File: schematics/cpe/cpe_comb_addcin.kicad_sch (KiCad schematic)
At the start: 9 parts

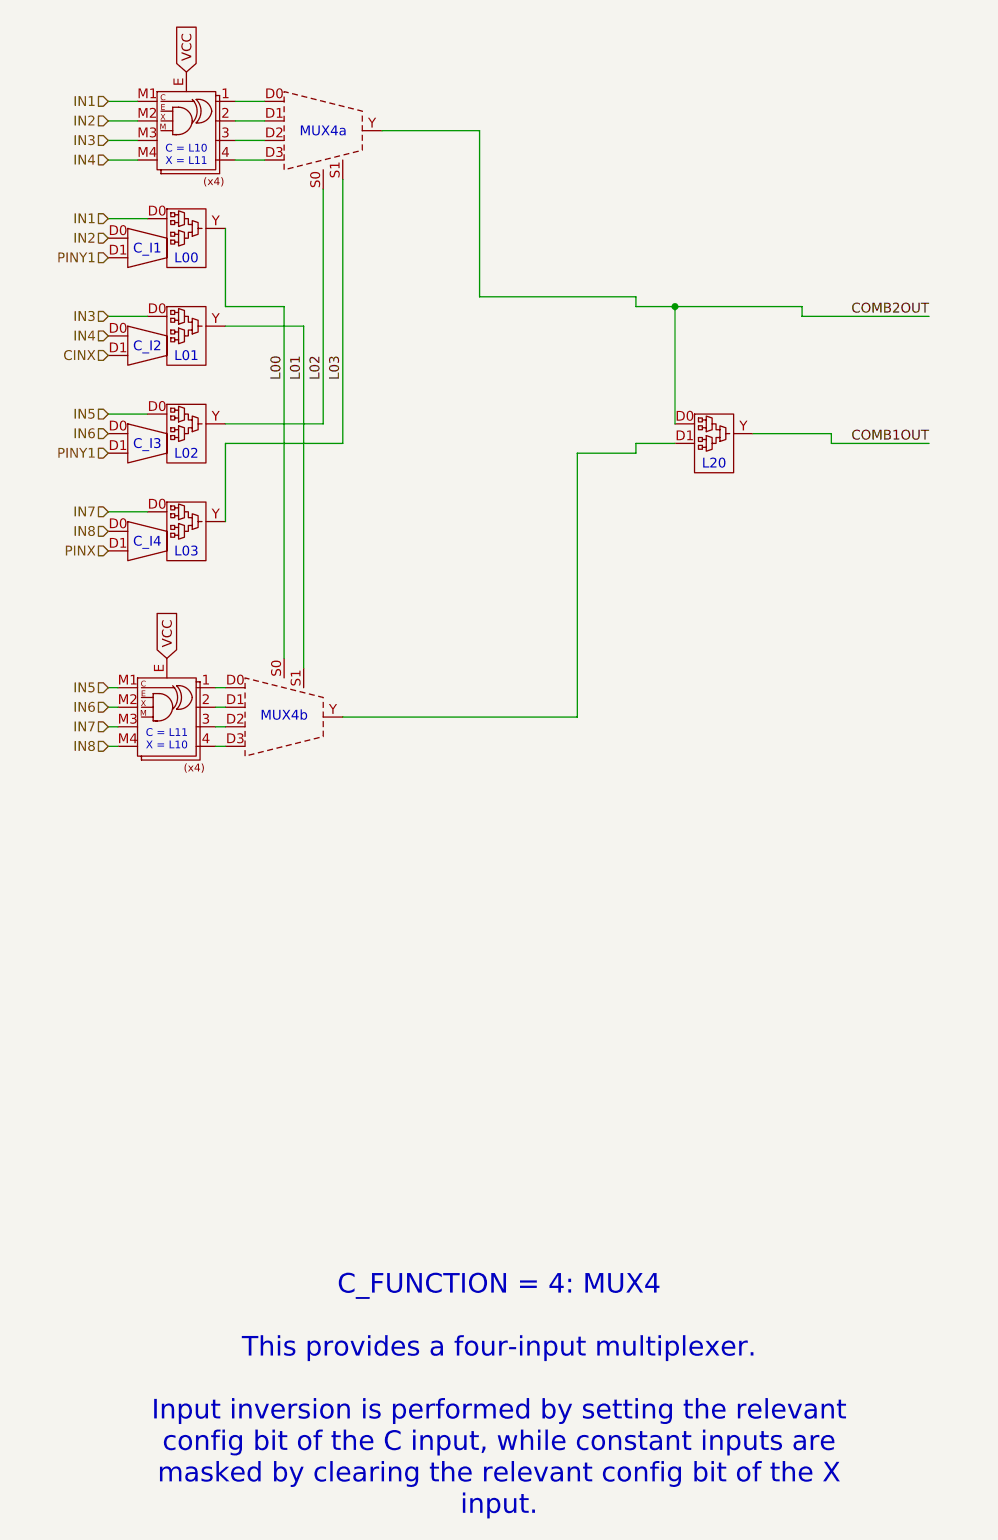
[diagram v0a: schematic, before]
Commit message: further CPE schematic updates
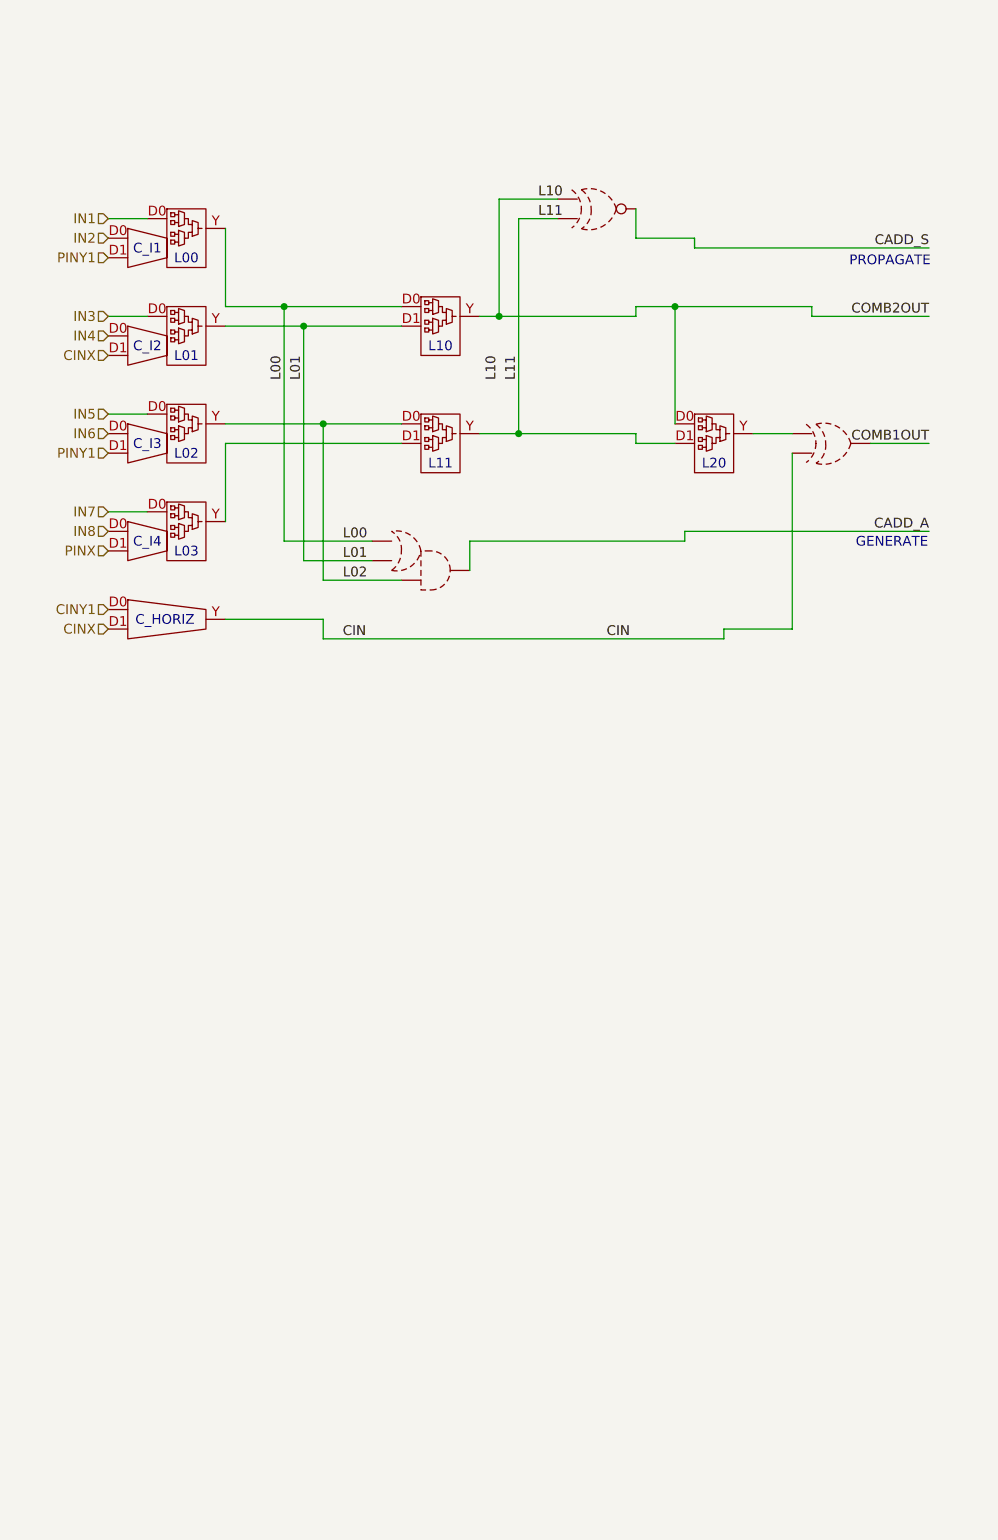
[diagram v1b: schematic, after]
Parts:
- removed INIT_L15, INIT_L16, INIT_L17, L20: ~, symbol peppercorn:LUT2 with C_I mux
- removed L23: ~, symbol peppercorn:LUT2
- removed M12: ~, symbol peppercorn:MUX4 (conceptual)
- removed M13: ~, symbol peppercorn:MUX4 (conceptual) (upside down)
- removed U6, U7: ~, symbol peppercorn:MUX invert/mask
- added C5: ~, symbol peppercorn:MUX2B
- added INIT_L7, INIT_L8, INIT_L9, L12: ~, symbol peppercorn:LUT2 with C_I mux
- added L13, L14, L15: ~, symbol peppercorn:LUT2
- added U59: ~, symbol peppercorn:AO21
- added U61: ~, symbol peppercorn:XNOR
- added U71: ~, symbol peppercorn:XOR
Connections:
- net CINX: now also C5.D1, INIT_L7.D1
- net COMB1OUT: now also U71.
- net COMB2OUT: now also L13.Y, L15.D0, U61.
- net IN1: now also L12.D0
- net IN2: now also L12.D0
- net IN3: now also INIT_L7.D0
- net IN4: now also INIT_L7.D0
- net IN5: now also INIT_L8.D0
- net IN6: now also INIT_L8.D0
- net IN7: now also INIT_L9.D0
- net IN8: now also INIT_L9.D0
- net L00: now also L12.Y, L13.D0, U59.
- net L01: now also INIT_L7.Y, L13.D1, U59.
- net L02: now also INIT_L8.Y, L14.D0, U59.
- net PINX: now also INIT_L9.D1
- net PINY1: now also INIT_L8.D1, L12.D1
- new net: INIT_L9.Y, L14.D1
- new net: L15.Y, U71.
- new net CADD_A: U59.
- new net CADD_S: U61.
- new net CIN: C5.Y, U71.
- new net CINY1: C5.D0
- new net L11: L14.Y, L15.D1, U61.
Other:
- note added: "C_HORIZ"
- note added: "GENERATE"
- note added: "L10"
- note added: "L11"
- note added: "PROPAGATE"
- note removed: "C = L10 X = L11"
- note removed: "C = L11 X = L10"
- note removed: "C_FUNCTION = 4: MUX4 This provides a four-input multiplexer. Input inversion is performed by setting the relevant config bit of the C input, while constant inputs are masked by clearing the relevant config bit of the X input."
- note removed: "MUX4a"
- note removed: "MUX4b"
- title: CPE: 4-Input Multiplexer Mode -> CPE: Sum Output With Carry
